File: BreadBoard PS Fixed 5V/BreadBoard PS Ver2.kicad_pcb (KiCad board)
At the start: 2 copper layers, 29.8 x 52 mm, 15 parts, among them J1 Barrel_Jack_Switch_MountingPin, J2 Conn_02x02_Odd_Even, J3 Conn_02x02_Odd_Even, J4 Conn_02x02_Odd_Even, J5 Conn_02x02_Odd_Even, SW1 SW_DPDT_x2, U1 LM7805_TO220

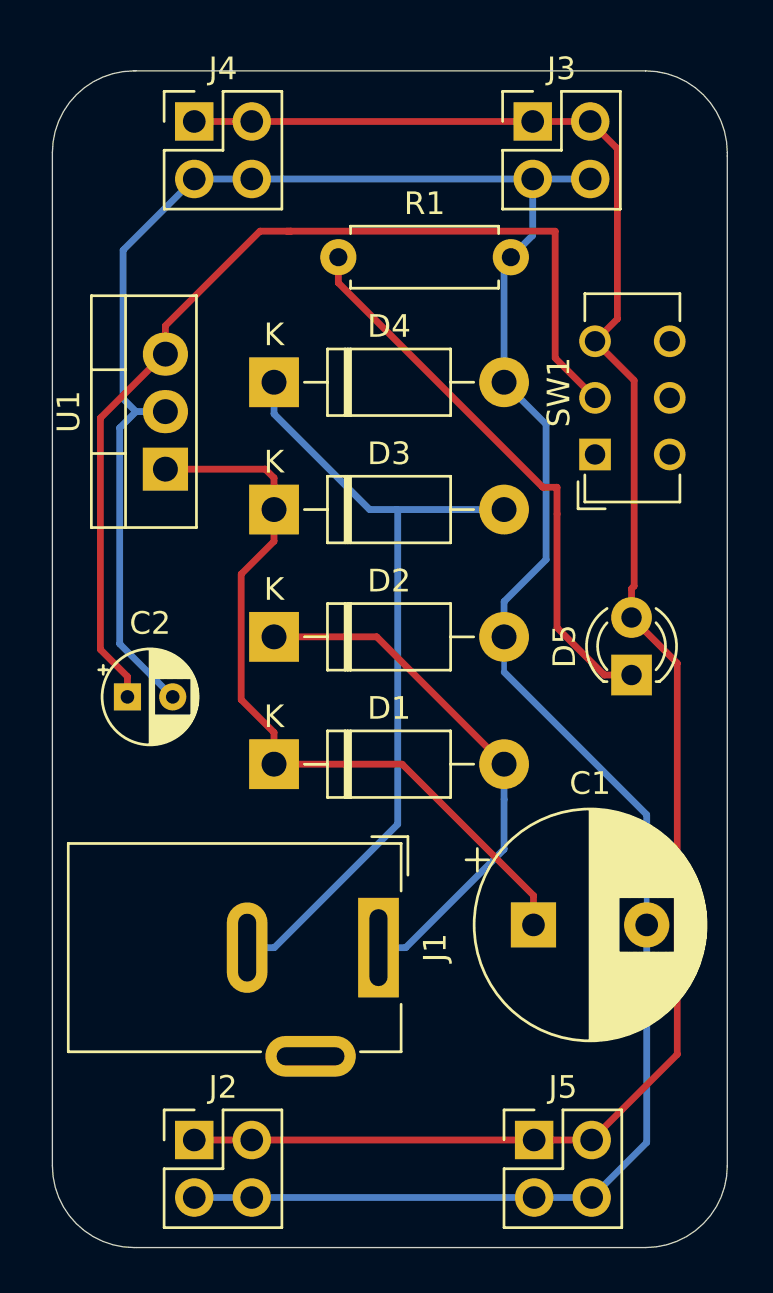
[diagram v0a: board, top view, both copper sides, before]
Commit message: add logos
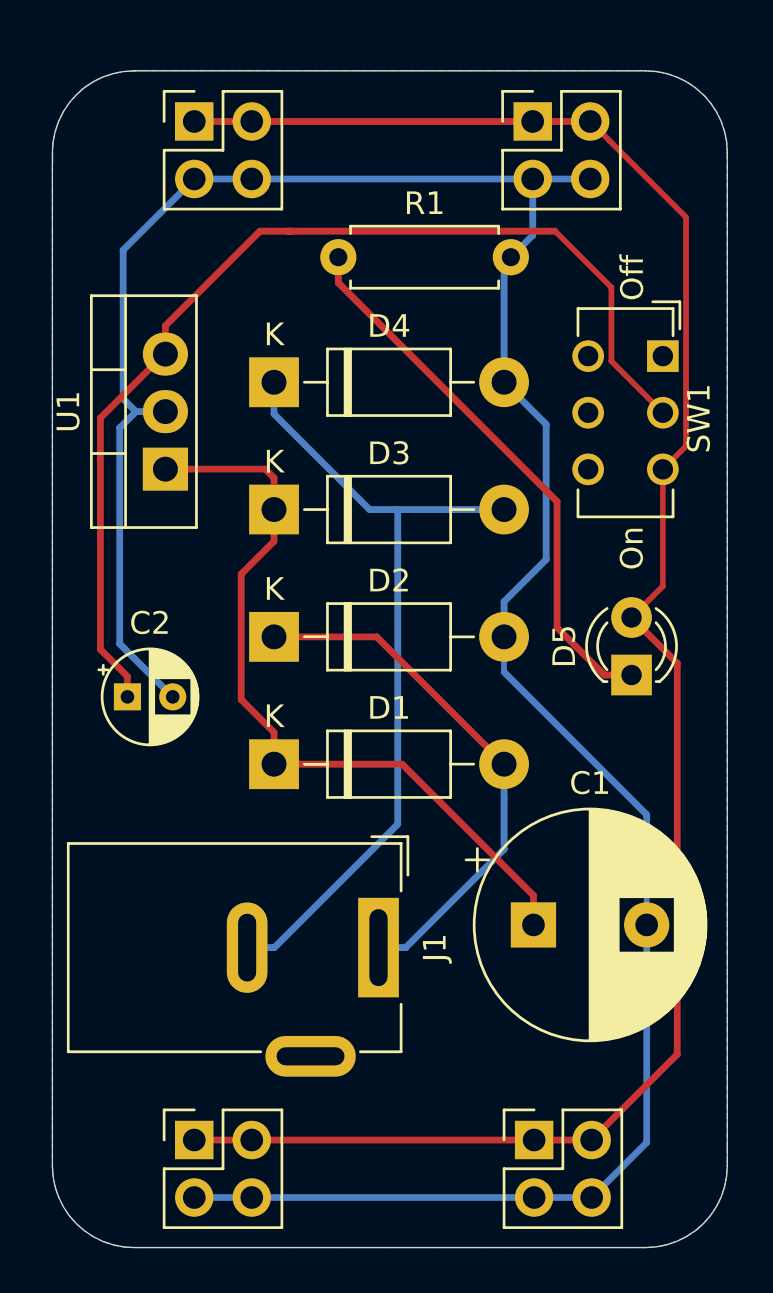
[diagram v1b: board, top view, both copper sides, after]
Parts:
- added G***: LOGO, Kicad:TSL logo 13mm x 9mm, B.Cu at (147.7, 111.0)
- added G***: LOGO, Kicad:TNT Logo 12.6mm x 7mm, B.Cu at (156.0, 97.2)
- moved SW1 5.28 mm to (168.1, 84.7), turned to 270 degrees
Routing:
- net /5V: track 45.3 -> 47.2 mm
- net /5V-out: track 84.1 -> 85.2 mm
- added copper zone on B.Cu, net /Gnd
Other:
- board text added: "Breadboard PS Fixed 5V v2 Timothy S Leishman 12/3/21"
- board text added: "Off"
- board text added: "On"
- board text added: "https://github.com/leistimo/Breadboard-Powersupply"

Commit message: generate gerber files
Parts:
- moved C2 3.09 mm to (144.4, 96.6)
- moved J1 1.70 mm to (157.2, 111.0)
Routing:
- net /5V: track 47.2 -> 44.1 mm
- net /Gnd: track 113.9 -> 110.8 mm
- net Net-(D3-Pad2): track 36.2 -> 35.2 mm
- net Net-(D1-Pad2): track 23.6 -> 23.1 mm
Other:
- board text added: "5V Rail"
- board text added: "6V to 35V (Do not exceed 35V)"
- board text added: "Breadboard PS Fixed 5V v2 Timothy S Leishman 12/6/21"
- board text added: "GND Rail"
- board text removed: "Breadboard PS Fixed 5V v2 Timothy S Leishman 12/3/21"
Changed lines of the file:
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@@
   (general
     (thickness 1.6)
-    (drawings 15)
-    (tracks 87)
+    (drawings 20)
+    (tracks 88)
     (zones 0)
     (modules 17)
@@
   )
   (setup
-    (last_trace_width 0.25)
+    (last_trace_width 0.3)
     (user_trace_width 0.3)
     (trace_clearance 0.2)
@@
     (pcbplotparams
       (layerselection 0x010fc_ffffffff)
-      (usegerberextensions false)
+      (usegerberextensions true)
       (usegerberattributes false)
       (usegerberadvancedattributes false)
@@
       (outputformat 1)
       (mirror false)
-      (drillshape 1)
+      (drillshape 0)
       (scaleselection 1)
-      (outputdirectory ""))
+      (outputdirectory "Gerber/"))
   )
   (net 0 "")
@@
   )
   (module Capacitor_THT:CP_Radial_D4.0mm_P2.00mm (layer F.Cu)
-    (at 144.4371 99.7204)
+    (at 144.4117 96.6343)
     (descr "CP, Radial series, Radial, pin pitch=2.00mm, , diameter=4mm, Electrolytic Capacitor")
     (tags "CP Radial series Radial pin pitch 2.00mm  diameter 4mm Electrolytic Capacitor")
@@
   )
   (module Connector_BarrelJack:BarrelJack_Wuerth_6941xx301002 (layer F.Cu)
-    (at 155.5242 110.7948 270)
+    (at 157.2133 110.9599 270)
     (descr "Wuerth electronics barrel jack connector (5.5mm outher diameter, inner diameter 2.05mm or 2.55mm depending on exact order number), See: http://katalog.we-online.de/em/datasheet/6941xx301002.pdf")
     (tags "connector barrel jack")
-    (fp_text reference J1 (at 0 -2.5 90) (layer F.SilkS)
+    (fp_text reference J1 (at 0.127 3.0226 90) (layer F.SilkS)
       (effects (font (size 1 1) (thickness 0.15)))
     )
@@
     (descr "Resistor, Axial_DIN0207 series, Axial, Horizontal, pin pitch=7.62mm, 0.25W = 1/4W, length*diameter=6.3*2.5mm^2, http://cdn-reichelt.de/documents/datenblatt/B400/1_4W%23YAG.pdf")
     (tags "Resistor Axial_DIN0207 series Axial Horizontal pin pitch 7.62mm 0.25W = 1/4W length 6.3mm diameter 2.5mm")
-    (fp_text reference R1 (at 3.81 -2.37) (layer F.SilkS)
+    (fp_text reference R1 (at 4.7323 2.2352) (layer F.SilkS)
       (effects (font (size 1 1) (thickness 0.15)))
     )
@@
     )
   )
+  (gr_text "5V Rail" (at 156.0195 74.2696 180) (layer F.SilkS)
+    (effects (font (size 1 1) (thickness 0.15)))
+  )
+  (gr_text "GND Rail" (at 156.1973 76.835 180) (layer F.SilkS)
+    (effects (font (size 1 1) (thickness 0.15)))
+  )
+  (gr_text "GND Rail" (at 155.956 121.7676) (layer F.SilkS)
+    (effects (font (size 1 1) (thickness 0.15)))
+  )
+  (gr_text "5V Rail" (at 156.1211 119.2403) (layer F.SilkS)
+    (effects (font (size 1 1) (thickness 0.15)))
+  )
+  (gr_text "6V to 35V (Do not exceed 35V)" (at 142.2273 109.5756 270) (layer F.SilkS)
+    (effects (font (size 1 1) (thickness 0.15)))
+  )
   (gr_text https://github.com/leistimo/Breadboard-Powersupply (at 169.5831 98.0059 90) (layer B.SilkS)
     (effects (font (size 1 1) (thickness 0.15)) (justify mirror))
@@
     (effects (font (size 1 1) (thickness 0.15)))
   )
-  (gr_text "Breadboard PS Fixed 5V v2\nTimothy S Leishman 12/3/21\n" (at 143.5608 100.6475 90) (layer B.SilkS)
+  (gr_text "Breadboard PS Fixed 5V v2\nTimothy S Leishman 12/6/21\n" (at 143.5608 100.6475 90) (layer B.SilkS)
     (effects (font (size 1 1) (thickness 0.15)) (justify left mirror))
   )
@@
   (segment (start 144.8135 87.122) (end 146.1135 87.122) (width 0.3) (layer B.Cu) (net 2))
   (segment (start 144.0942 87.8413) (end 144.8135 87.122) (width 0.3) (layer B.Cu) (net 2))
-  (segment (start 144.0942 97.3775) (end 144.0942 87.8413) (width 0.3) (layer B.Cu) (net 2))
-  (segment (start 146.4371 99.7204) (end 144.0942 97.3775) (width 0.3) (layer B.Cu) (net 2))
   (segment (start 146.1135 87.122) (end 144.8635 87.122) (width 0.25) (layer B.Cu) (net 2))
   (segment (start 144.8135 87.122) (end 144.2466 86.5551) (width 0.3) (layer B.Cu) (net 2))
@@
   (segment (start 144.2466 86.5551) (end 144.2466 79.9886) (width 0.3) (layer B.Cu) (net 2))
   (segment (start 149.9275 121.8311) (end 147.3875 121.8311) (width 0.3) (layer B.Cu) (net 2))
-  (segment (start 144.4371 98.8204) (end 143.2433 97.6266) (width 0.3) (layer F.Cu) (net 3))
-  (segment (start 144.4371 99.7204) (end 144.4371 98.8204) (width 0.3) (layer F.Cu) (net 3))
-  (segment (start 146.066 84.582) (end 146.1135 84.582) (width 0.3) (layer F.Cu) (net 3))
-  (segment (start 143.2433 87.4047) (end 146.066 84.582) (width 0.3) (layer F.Cu) (net 3))
-  (segment (start 143.2433 97.6266) (end 143.2433 87.4047) (width 0.3) (layer F.Cu) (net 3))
+  (segment (start 144.0942 93.468272) (end 144.0942 87.8413) (width 0.3) (layer B.Cu) (net 2))
+  (segment (start 146.4117 95.785772) (end 144.0942 93.468272) (width 0.3) (layer B.Cu) (net 2))
+  (segment (start 146.4117 96.6343) (end 146.4117 95.785772) (width 0.3) (layer B.Cu) (net 2))
   (segment (start 150.290901 79.152099) (end 151.656399 79.152099) (width 0.3) (layer F.Cu) (net 3))
   (segment (start 146.1135 83.3295) (end 150.290901 79.152099) (width 0.3) (layer F.Cu) (net 3))
@@
   (segment (start 165.809501 84.895901) (end 165.809501 81.633901) (width 0.25) (layer F.Cu) (net 3))
   (segment (start 168.0845 87.1709) (end 165.809501 84.895901) (width 0.25) (layer F.Cu) (net 3))
-  (segment (start 161.071 104.247834) (end 161.071 102.6922) (width 0.3) (layer B.Cu) (net 4))
-  (segment (start 161.071 106.448) (end 161.071 104.247834) (width 0.3) (layer B.Cu) (net 4))
-  (segment (start 156.7242 110.7948) (end 161.071 106.448) (width 0.3) (layer B.Cu) (net 4))
-  (segment (start 155.5242 110.7948) (end 156.7242 110.7948) (width 0.3) (layer B.Cu) (net 4))
+  (segment (start 144.4117 95.7343) (end 144.4117 96.6343) (width 0.3) (layer F.Cu) (net 3))
+  (segment (start 143.2433 94.5659) (end 144.4117 95.7343) (width 0.3) (layer F.Cu) (net 3))
+  (segment (start 143.2433 87.4047) (end 143.2433 94.5659) (width 0.3) (layer F.Cu) (net 3))
+  (segment (start 146.1135 84.582) (end 146.066 84.582) (width 0.3) (layer F.Cu) (net 3))
+  (segment (start 146.066 84.582) (end 143.2433 87.4047) (width 0.3) (layer F.Cu) (net 3))
   (segment (start 155.448475 97.069675) (end 161.071 102.6922) (width 0.3) (layer F.Cu) (net 4))
   (segment (start 150.911 97.069675) (end 155.448475 97.069675) (width 0.3) (layer F.Cu) (net 4))
+  (segment (start 161.071 104.247834) (end 161.071 102.6922) (width 0.3) (layer B.Cu) (net 4))
+  (segment (start 161.071 108.3022) (end 161.071 104.247834) (width 0.3) (layer B.Cu) (net 4))
+  (segment (start 158.4133 110.9599) (end 161.071 108.3022) (width 0.3) (layer B.Cu) (net 4))
+  (segment (start 157.2133 110.9599) (end 158.4133 110.9599) (width 0.3) (layer B.Cu) (net 4))
   (segment (start 150.911 87.224625) (end 150.911 85.824625) (width 0.3) (layer B.Cu) (net 5))
   (segment (start 155.133525 91.44715) (end 150.911 87.224625) (width 0.3) (layer B.Cu) (net 5))
@@
   (segment (start 161.071 91.44715) (end 156.32985 91.44715) (width 0.3) (layer B.Cu) (net 5))
   (segment (start 156.3751 91.4924) (end 156.32985 91.44715) (width 0.3) (layer B.Cu) (net 5))
-  (segment (start 156.3751 105.3439) (end 156.3751 91.4924) (width 0.3) (layer B.Cu) (net 5))
-  (segment (start 149.7242 110.7948) (end 150.9242 110.7948) (width 0.3) (layer B.Cu) (net 5))
-  (segment (start 150.9242 110.7948) (end 156.3751 105.3439) (width 0.3) (layer B.Cu) (net 5))
+  (segment (start 155.133525 108.439675) (end 155.133525 91.44715) (width 0.3) (layer B.Cu) (net 5))
+  (segment (start 152.6133 110.9599) (end 155.133525 108.439675) (width 0.3) (layer B.Cu) (net 5))
+  (segment (start 151.4133 110.9599) (end 152.6133 110.9599) (width 0.3) (layer B.Cu) (net 5))
   (segment (start 153.751 81.43347) (end 153.751 80.3021) (width 0.3) (layer F.Cu) (net 6))
   (segment (start 163.4109 91.09337) (end 153.751 81.43347) (width 0.3) (layer F.Cu) (net 6))

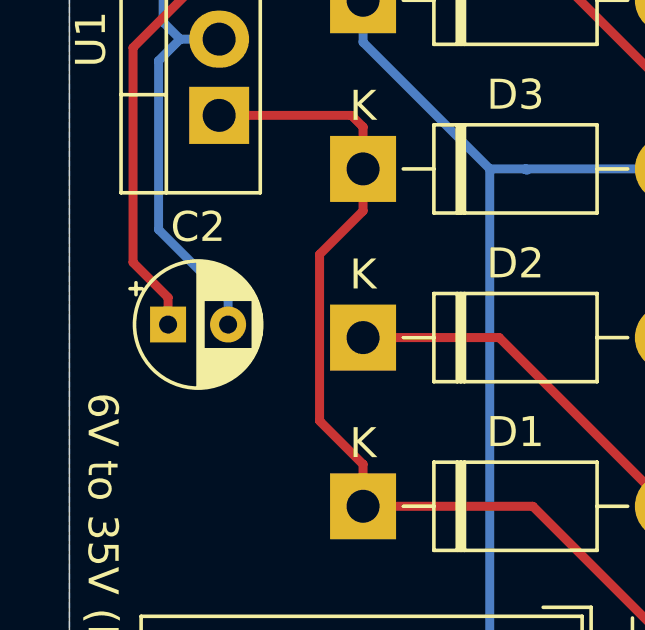
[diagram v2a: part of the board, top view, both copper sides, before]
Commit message: Update C2 footprint
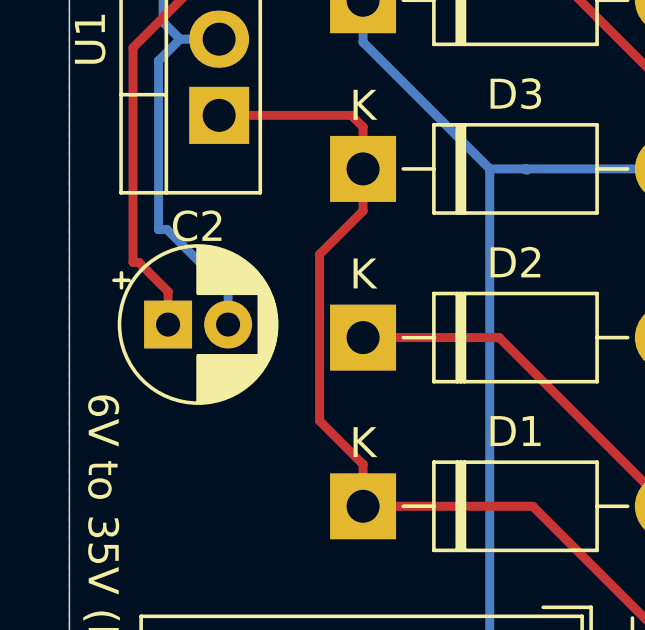
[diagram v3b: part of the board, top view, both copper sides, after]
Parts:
- C2: footprint Capacitor_THT:CP_Radial_D4.0mm_P2.00mm -> Capacitor_THT:CP_Radial_D5.0mm_P2.00mm
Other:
- board text added: "Breadboard PS Fixed 5V v2 Timothy S Leishman 12/8/21"
- board text removed: "Breadboard PS Fixed 5V v2 Timothy S Leishman 12/6/21"

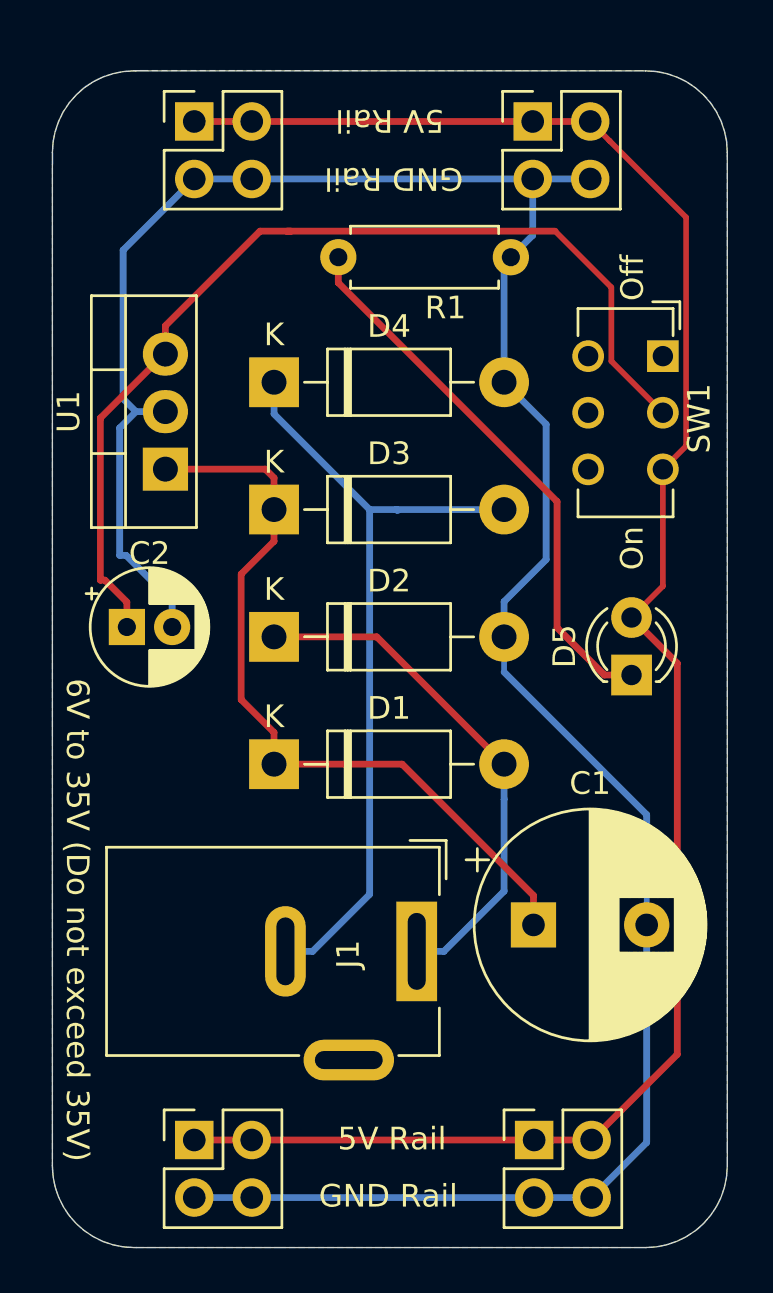
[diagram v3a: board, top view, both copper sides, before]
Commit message: update rail pin locations
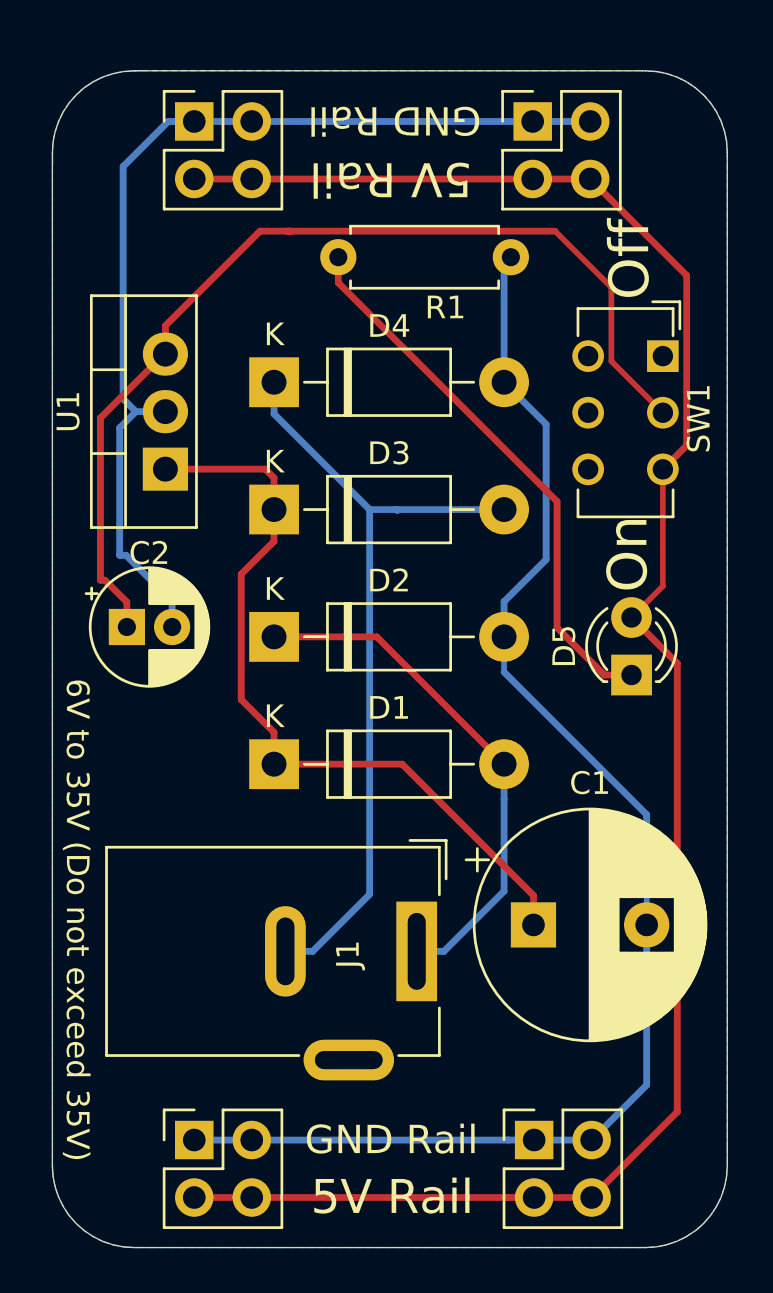
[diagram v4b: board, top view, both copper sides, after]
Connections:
- J2 pad 1: /5V-out -> /Gnd
- J2 pad 2: /5V-out -> /Gnd
- J2 pad 3: /Gnd -> /5V-out
- J2 pad 4: /Gnd -> /5V-out
- J3 pad 1: /5V-out -> /Gnd
- J3 pad 2: /5V-out -> /Gnd
- J3 pad 3: /Gnd -> /5V-out
- J3 pad 4: /Gnd -> /5V-out
- J4 pad 1: /5V-out -> /Gnd
- J4 pad 2: /5V-out -> /Gnd
- J4 pad 3: /Gnd -> /5V-out
- J4 pad 4: /Gnd -> /5V-out
- J5 pad 1: /5V-out -> /Gnd
- J5 pad 2: /5V-out -> /Gnd
- J5 pad 3: /Gnd -> /5V-out
- J5 pad 4: /Gnd -> /5V-out
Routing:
- net /Gnd: track 111.0 -> 107.8 mm
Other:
- board text added: "Breadboard PS Fixed 5V v2 Timothy S Leishman 12/19/21"
- board text removed: "Breadboard PS Fixed 5V v2 Timothy S Leishman 12/8/21"
